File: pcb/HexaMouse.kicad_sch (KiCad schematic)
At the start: 0 parts

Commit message: Added microcontroller board to schematic
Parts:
- added U1: XIAO-nRF52840-SMD, Seeed_Studio_XIAO_Series:XIAO-nRF52840-SMD, symbol Seeed_Studio_XIAO_Series:XIAO-nRF52840-SMD
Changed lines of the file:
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@@
 	(generator_version "10.0")
 	(paper "A4")
+	(symbol
+		(lib_id "Seeed_Studio_XIAO_Series:XIAO-nRF52840-SMD")
+		(at 148.59 99.06 0)
+		(unit 1)
+		(body_style 1)
+		(exclude_from_sim no)
+		(in_bom yes)
+		(on_board yes)
+		(in_pos_files yes)
+		(dnp no)
+		(fields_autoplaced yes)
+		(property "Reference" "U1"
+			(at 154.5433 69.85 0)
+			(show_name no)
+			(do_not_autoplace no)
+			(effects
+				(font
+					(size 1.27 1.27)
+				)
+				(justify left)
+			)
+		)
+		(property "Value" "XIAO-nRF52840-SMD"
+			(at 154.5433 72.39 0)
+			(show_name no)
+			(do_not_autoplace no)
+			(effects
+				(font
+					(size 1.27 1.27)
+				)
+				(justify left)
+			)
+		)
+		(property "Footprint" "Seeed_Studio_XIAO_Series:XIAO-nRF52840-SMD"
+			(at 139.7 93.98 0)
+			(hide yes)
+			(show_name no)
+			(do_not_autoplace no)
+			(effects
+				(font
+					(size 1.27 1.27)
+				)
+			)
+		)
+		(property "Datasheet" ""
+			(at 139.7 93.98 0)
+			(hide yes)
+			(show_name no)
+			(do_not_autoplace no)
+			(effects
+				(font
+					(size 1.27 1.27)
+				)
+			)
+		)
+		(property "Description" ""
+			(at 148.59 99.06 0)
+			(hide yes)
+			(show_name no)
+			(do_not_autoplace no)
+			(effects
+				(font
+					(size 1.27 1.27)
+				)
+			)
+		)
+		(pin "8"
+		)
+		(pin "15"
+		)
+		(pin "21"
+		)
+		(pin "14"
+		)
+		(pin "2"
+		)
+		(pin "20"
+		)
+		(pin "13"
+		)
+		(pin "19"
+		)
+		(pin "11"
+		)
+		(pin "17"
+		)
+		(pin "18"
+		)
+		(pin "12"
+		)
+		(pin "7"
+		)
+		(pin "16"
+		)
+		(pin "3"
+		)
+		(pin "9"
+		)
+		(pin "1"
+		)
+		(pin "4"
+		)
+		(pin "22"
+		)
+		(pin "6"
+		)
+		(pin "5"
+		)
+		(pin "10"
+		)
+		(instances
+			(project "HexaMouse"
+				(path "/deae72d5-0817-48b9-87be-e09fd68b7fc0"
+					(reference "U1")
+					(unit 1)
+				)
+			)
+		)
+	)
 	(sheet_instances
 		(path "/"

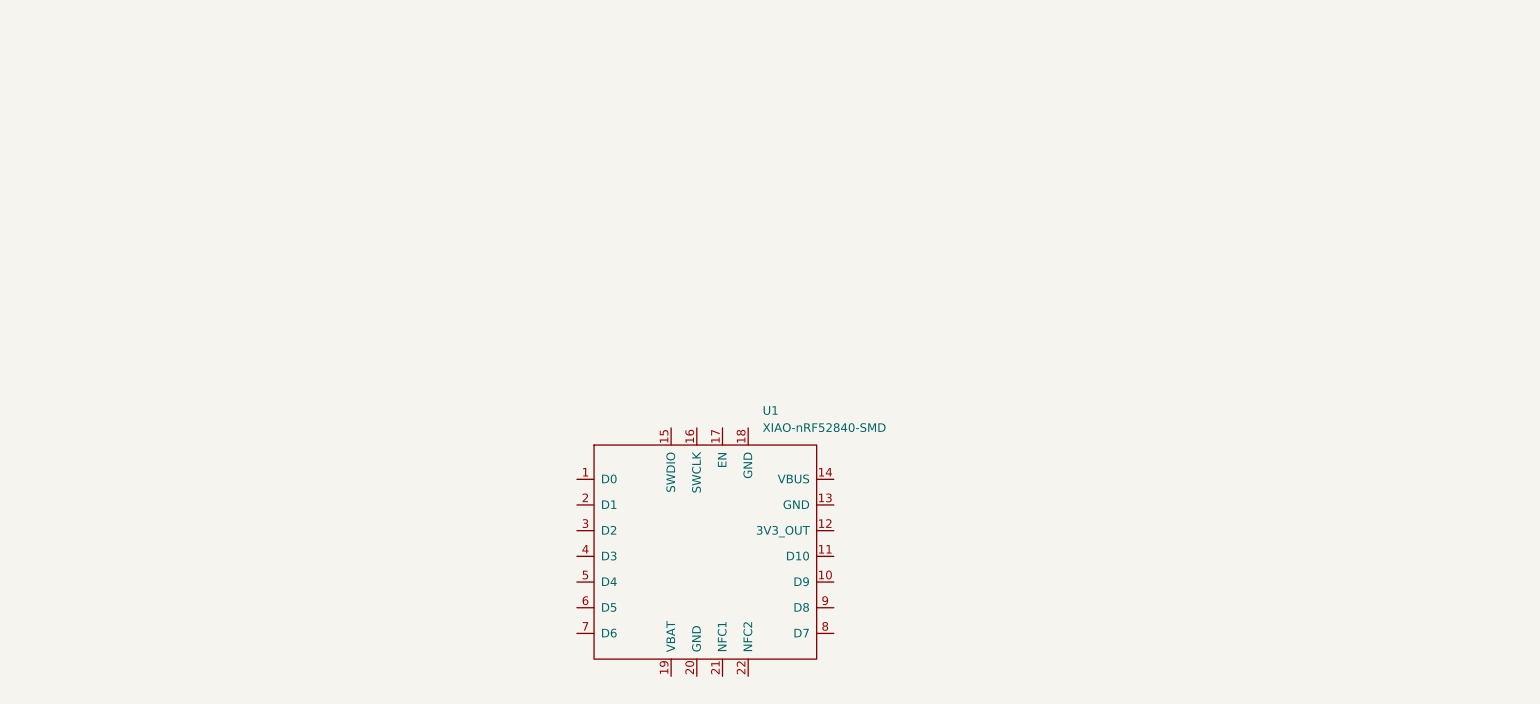
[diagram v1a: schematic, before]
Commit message: magnetometers + i2c mux added to schematic
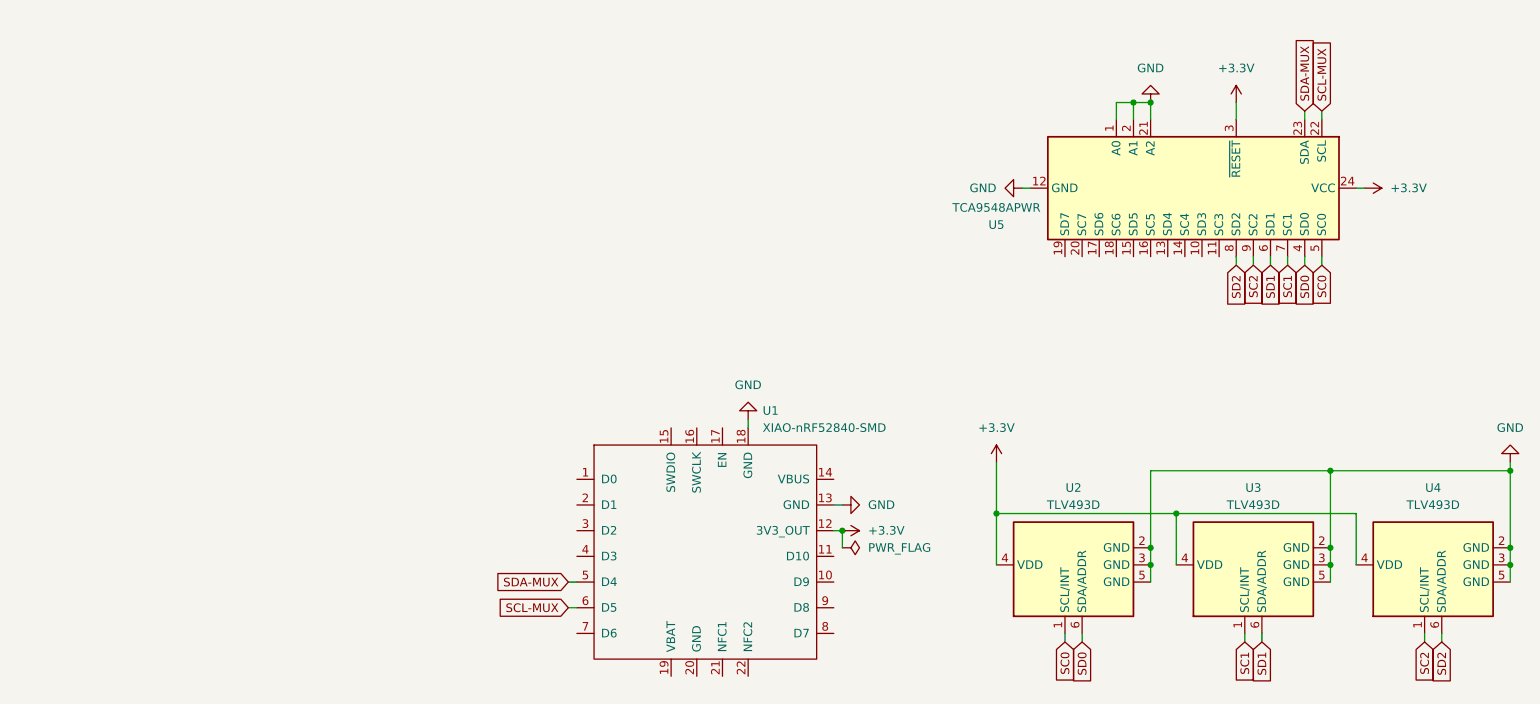
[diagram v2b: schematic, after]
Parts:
- added U2, U3, U4: TLV493D, Package_TO_SOT_SMD:SOT-23-6, symbol Sensor_Magnetic:TLV493D
- added U5: TCA9548APWR, Package_SO:TSSOP-24_4.4x7.8mm_P0.65mm, symbol Interface_Expansion:TCA9548APWR
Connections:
- net +3.3V: now reaches U1.12 (3V3_OUT)
- net +3.3V: now also U2.4 (VDD), U3.4 (VDD), U4.4 (VDD), U5.24 (VCC), U5.3 (~{RESET})
- net GND: now reaches U1.13 (GND)
- net GND: now also U1.18 (GND), U2.2 (GND), U2.3 (GND), U2.5 (GND), U3.2 (GND), U3.3 (GND), U3.5 (GND), U4.2 (GND), U4.3 (GND), U4.5 (GND), U5.1 (A0), U5.12 (GND), U5.2 (A1), U5.21 (A2)
- net SDA-MUX: now reaches U1.5 (D4)
- net SDA-MUX: now also U5.23 (SDA)
- net SCL-MUX: now reaches U1.6 (D5)
- net SCL-MUX: now also U5.22 (SCL)
- new net SC0: U2.1 (SCL/INT), U5.5 (SC0)
- new net SC1: U3.1 (SCL/INT), U5.7 (SC1)
- new net SC2: U4.1 (SCL/INT), U5.9 (SC2)
- new net SD0: U2.6 (SDA/ADDR), U5.4 (SD0)
- new net SD1: U3.6 (SDA/ADDR), U5.6 (SD1)
- new net SD2: U4.6 (SDA/ADDR), U5.8 (SD2)

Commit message: Added supporting hardware
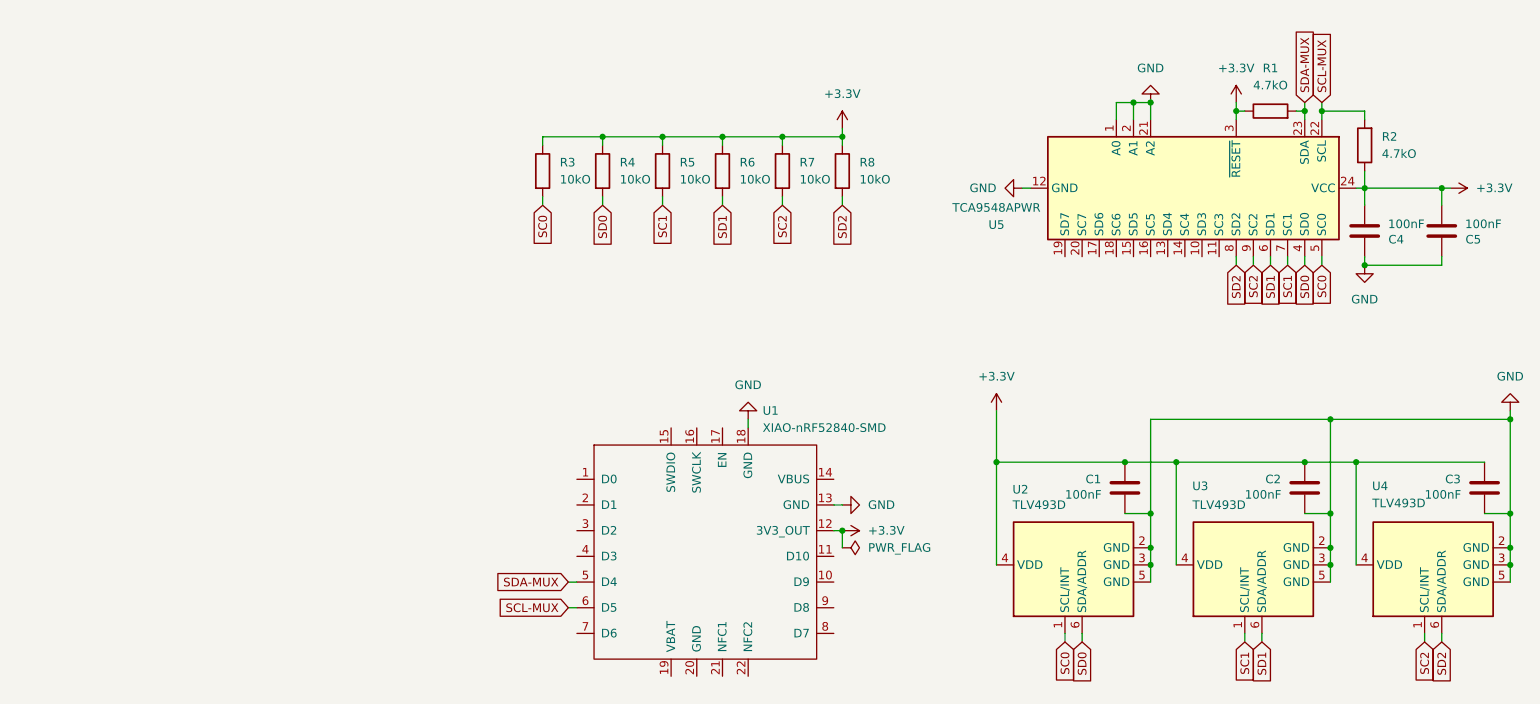
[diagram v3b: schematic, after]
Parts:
- added C1, C2, C3, C4, C5: 100nF, symbol Device:C
- added R1, R2: 4.7kO, Package_SO:TSSOP-24_4.4x7.8mm_P0.65mm, symbol Device:R
- added R3, R4, R5: 10kO, Package_SO:TSSOP-24_4.4x7.8mm_P0.65mm, symbol Device:R
- added R6, R7, R8: 10kO, symbol Device:R
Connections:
- net +3.3V: now also C1.1, C2.1, C3.1, C4.2, C5.2, R1.1, R2.1, R3.1, R4.1, R5.1, R6.1, R7.1, R8.1
- net GND: now also C1.2, C2.2, C3.2, C4.1, C5.1
- net SC0: now also R3.2
- net SC1: now also R5.2
- net SC2: now also R7.2
- net SCL-MUX: now also R2.2
- net SD0: now also R4.2
- net SD1: now also R6.2
- net SD2: now also R8.2
- net SDA-MUX: now also R1.2

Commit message: Added more power caps and no connect flags
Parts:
- added C6: 10uF, symbol Device:C
- added J1, J2: Conn_01x02_Socket, symbol Connector:Conn_01x02_Socket
- added SW1: SW_SPDT, Button_Switch_THT:SW_NKK_GW12LJP, symbol Switch:SW_SPDT
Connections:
- net +3.3V: now also C6.1
- net GND: now also C6.2
- new net: J1.1 (Pin_1), SW1.2 (B)
- new net: J1.2 (Pin_2), J2.1 (Pin_1)
- new net: J2.2 (Pin_2), SW1.1 (A)
- no-connect marks 0 -> 28
